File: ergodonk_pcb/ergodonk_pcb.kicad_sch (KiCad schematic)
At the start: 133 parts, among them J10 TRRS Double Sided, J11 Pimaroni Trackball, J12 Conn_01x04_Socket, Q1 TIP120, SW08_RH10 SW_PUSH_LED, SW1 SW_PUSH_LED, SW10 SW_PUSH_LED, SW11 SW_PUSH_LED, SW12 SW_PUSH_LED, SW13 SW_PUSH_LED, SW14 SW_PUSH_LED, SW15 SW_PUSH_LED, SW16 SW_PUSH_LED, SW17 SW_PUSH_LED, SW18_RH10 SW_PUSH_LED, SW2 SW_PUSH_LED, SW20 SW_PUSH_LED, SW21 SW_PUSH_LED, SW22 SW_PUSH_LED, SW23 SW_PUSH_LED, SW24 SW_PUSH_LED, SW25 SW_PUSH_LED, SW26 SW_PUSH_LED, SW27 SW_PUSH_LED, SW28_RH10 SW_PUSH_LED, SW3 SW_PUSH_LED, SW30 SW_PUSH_LED, SW31 SW_PUSH_LED, SW32 SW_PUSH_LED, SW33 SW_PUSH_LED, SW34 SW_PUSH_LED, SW35 SW_PUSH_LED, SW36 SW_PUSH_LED, SW37 SW_PUSH_LED, SW38_RH10 SW_PUSH_LED, SW4 SW_PUSH_LED, SW40 SW_PUSH_LED, SW42 SW_PUSH_LED, SW43 SW_PUSH_LED, SW44 SW_PUSH_LED, SW45 SW_PUSH_LED, SW46 SW_PUSH_LED, SW47 SW_PUSH_LED, SW48_RH10 SW_PUSH_LED, SW5 SW_PUSH_LED, SW50 SW_PUSH_LED, SW51 SW_PUSH_LED, SW52 SW_PUSH_LED, SW53 SW_PUSH_LED, SW54 SW_PUSH_LED, SW55 SW_PUSH_LED, SW56 SW_PUSH_LED, SW57 SW_PUSH_LED, SW58 SW_PUSH_LED, SW6 SW_PUSH_LED, SW7 SW_PUSH_LED, U10 Pico

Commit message: TRRS cleanup pimironi revision outline rework
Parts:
- removed J10: TRRS Double Sided, Resistor_SMD:R_1206_3216Metric_Pad1.30x1.75mm_HandSolder, symbol Ergodonk_symbols:TRRS_TX_to_RX_Doublesided_Crossover
- removed J11: Pimaroni Trackball, ergodonk_kicad_library:pimoroni_trackball, symbol Connector:Conn_01x05_Socket
- removed J12: Conn_01x04_Socket, symbol Connector:Conn_01x04_Socket
- added J1: TRRS, ergodonk_kicad_library:Cantor_DS_TRRS-PJ-320A, symbol keebio:TRRS
- added J10: Pimaroni Trackball, ergodonk_kicad_library:pimoroni_trackball, symbol Connector:Conn_01x05_Socket
- D_SOL_1: footprint Neffs_kicad_footprint_library:MUR340S_IN4004_TH -> kbd:R
- JP10: footprint (none) -> kbd:Jumper
- R12: footprint (none) -> kbd:R
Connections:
- net GND: now also J1.2 (TIP), J10.5 (Pin_5)
- net RX: now also J1.3 (RING1)
- net SCL: now also J10.3 (Pin_3)
- net SDA: now also J10.2 (Pin_2)
- net TX: now also J1.4 (RING2)
- net VCC: now also U10.36 (3V3); no longer U10.40 (VBUS)
- net at JP10.2 (B), R12.1: now also J10.1 (Pin_1)
- new net +3V3: J1.1 (SLEEVE)
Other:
- note added: "Todo: Check Pimaroni resistor calculation and footprint size Add holes to pimaroni footprint CHeck net trace sizes. (.5 for 3.3v?) Incree trcck size on vcc and GND nets Figure out VCC on Pico Figure out vbus_sense Cutouts for picon on PCB RH trackball Graphics Mouse bites Stabalizer holes Improve solenoid graphics Refactor key row/columns to put 00 in upper right for easier double sided Make Diod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"
- note removed: "Pimaroni Tie in (Additional Resistor?)"
- note removed: "Todo: pimaroni tie in additional pimroni resistor Incree trcck size on vcc and GND nets Figure out VCC on Pico Figure out vbus_sense Make new symbol for double sided TRRS Cutouts for picon on PCB Rewire for ProMicro footprint RH trackball Double sided RH/LH Add LEDs Graphics Mouse bites Stabalizer holes Improve solenoid graphics Refactor key row/columns to put 00 in upper right for easier double 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"

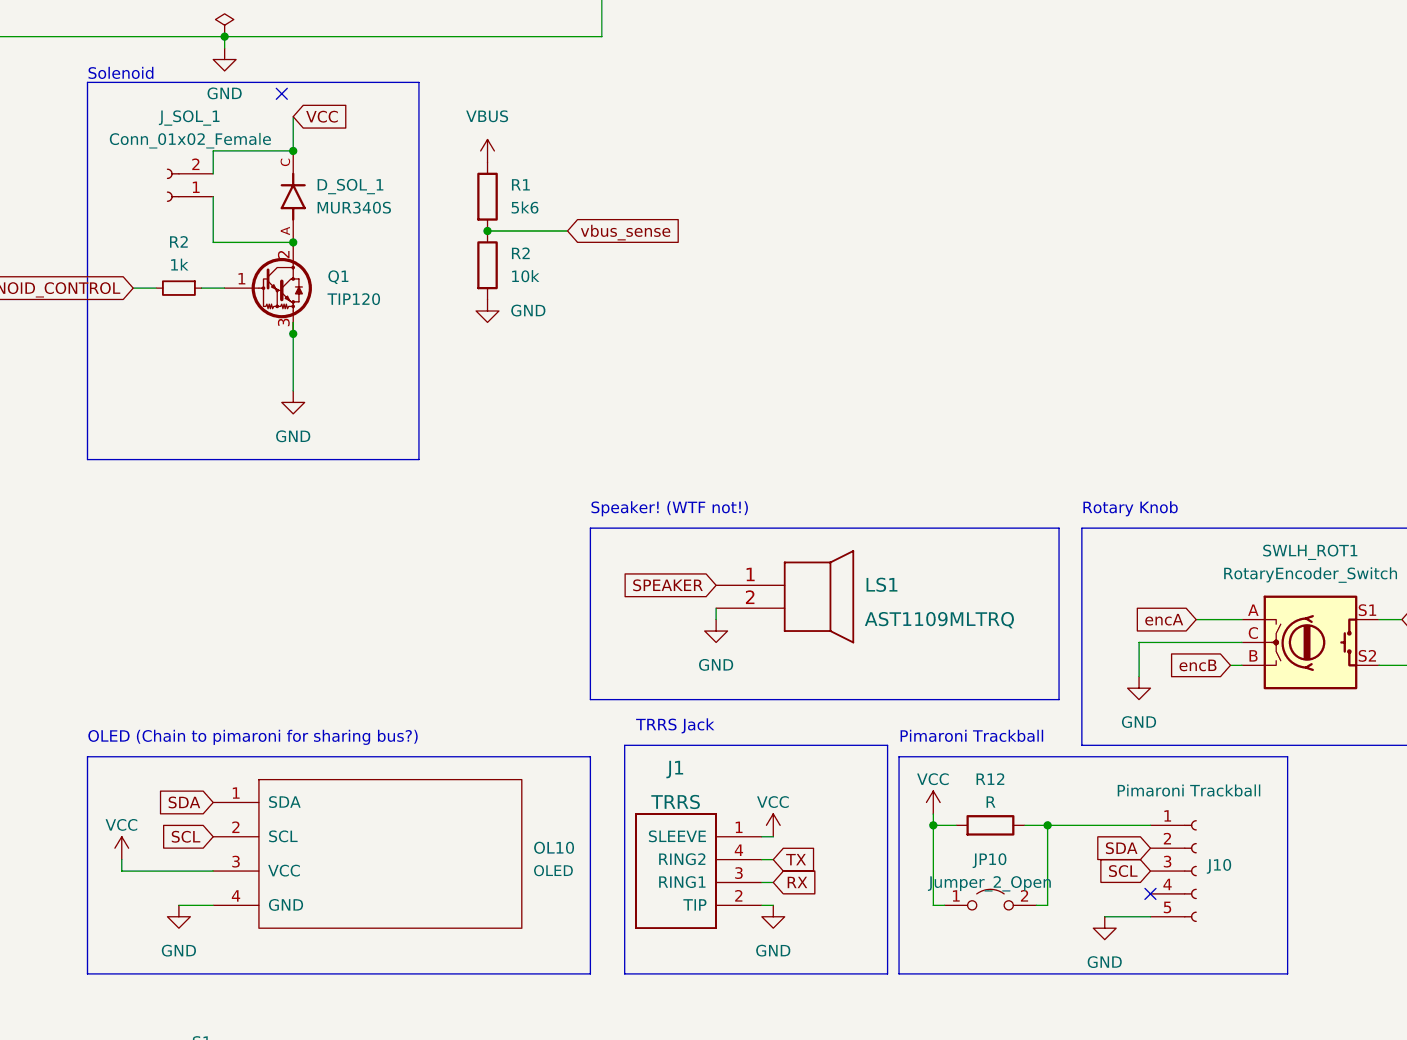
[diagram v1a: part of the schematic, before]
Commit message: Fixed MUR340 Hybrid footprint     Regenerated .dsn for autorouting
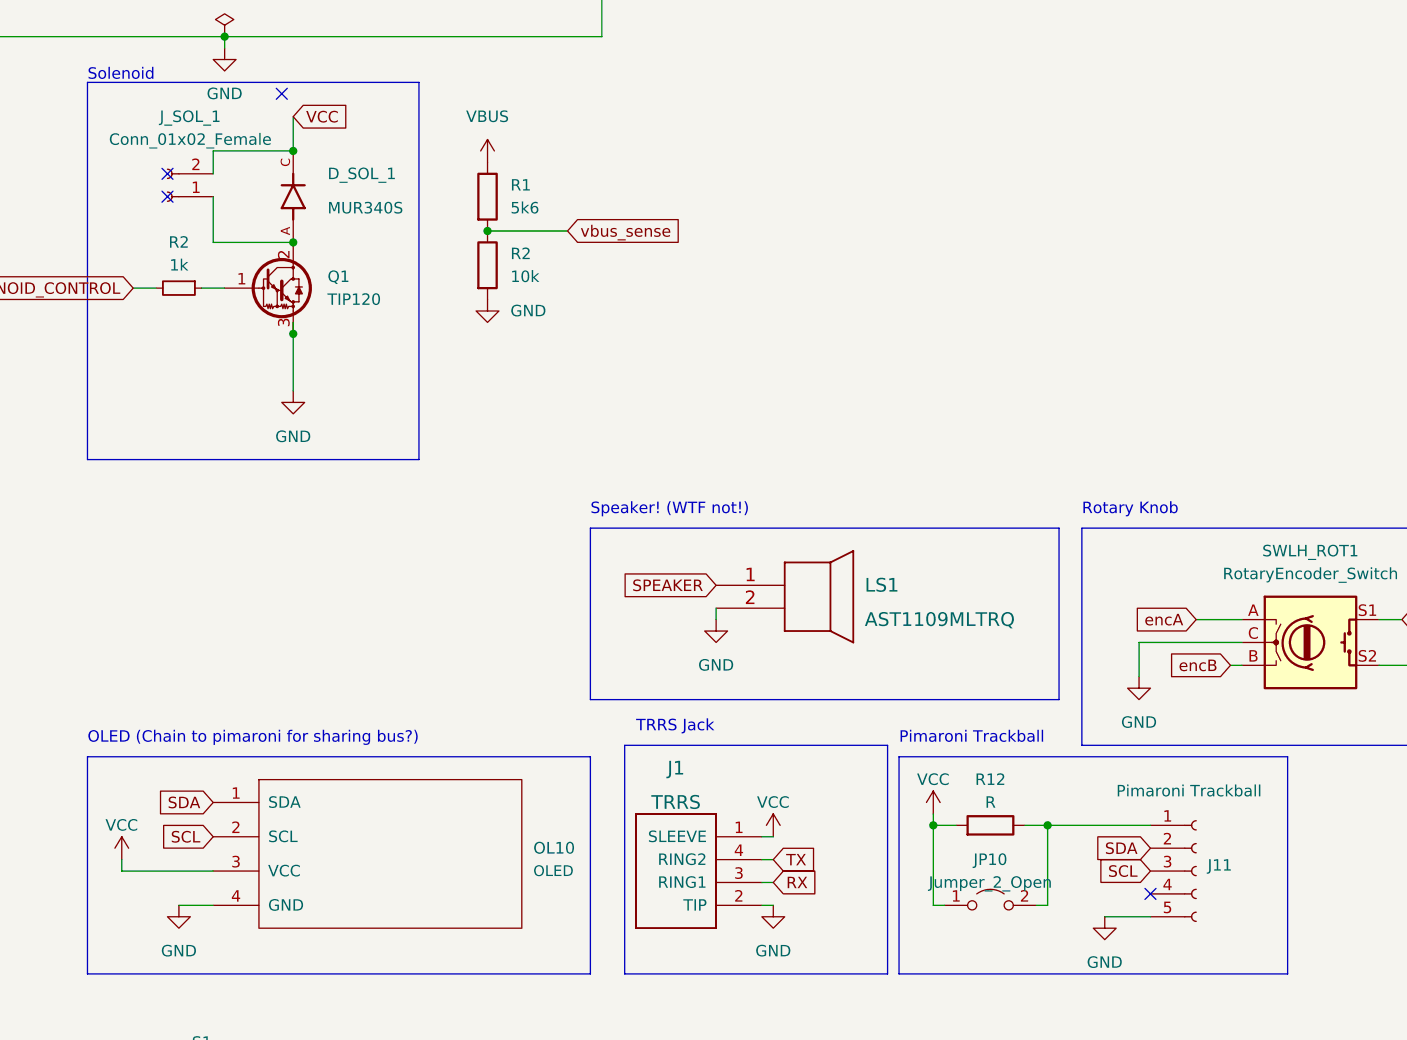
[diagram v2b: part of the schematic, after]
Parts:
- D_SOL_1: footprint kbd:R -> ergodonk_kicad_library:MUR340S_IN4004_TH
- renumbered J10 to J11
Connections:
- no-connect marks 2 -> 4
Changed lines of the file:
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@@
   )
   (no_connect (at 50.8 87.63))
+  (no_connect (at 38.1 99.06))
   (no_connect (at 147.32 176.53))
+  (no_connect (at 38.1 96.52))
   (wire (pts (xy 358.14 74.93) (xy 379.73 74.93))
     (stroke (width 0) (type default))
@@
   )
   (symbol (lib_id "MUR340S:MUR340S") (at 52.07 99.06 90) (unit 1)
-    (in_bom yes) (on_board yes) (dnp no) (fields_autoplaced)
-    (property "Reference" "D_SOL_1" (at 54.61 97.7899 90)
+    (in_bom yes) (on_board yes) (dnp no)
+    (property "Reference" "D_SOL_1" (at 55.88 96.52 90)
       (effects (font (size 1.27 1.27)) (justify right))
     )
-    (property "Value" "MUR340S" (at 54.61 100.3299 90)
+    (property "Value" "MUR340S" (at 55.88 100.33 90)
       (effects (font (size 1.27 1.27)) (justify right))
     )
-    (property "Footprint" "kbd:R" (at 52.07 99.06 0)
+    (property "Footprint" "ergodonk_kicad_library:MUR340S_IN4004_TH" (at 52.07 99.06 0)
       (effects (font (size 1.27 1.27)) (justify bottom) hide)
     )
@@
   (symbol (lib_id "Connector:Conn_01x05_Socket") (at 152.4 173.99 0) (unit 1)
     (in_bom yes) (on_board yes) (dnp no)
-    (property "Reference" "J10" (at 153.67 173.355 0)
+    (property "Reference" "J11" (at 153.67 173.355 0)
       (effects (font (size 1.27 1.27)) (justify left))
     )
@@
       (project "ergodonk_pcb"
         (path "/ed1aaf15-4e1f-4159-b371-d99b3fb972ad"
-          (reference "J10") (unit 1)
+          (reference "J11") (unit 1)
         )
       )

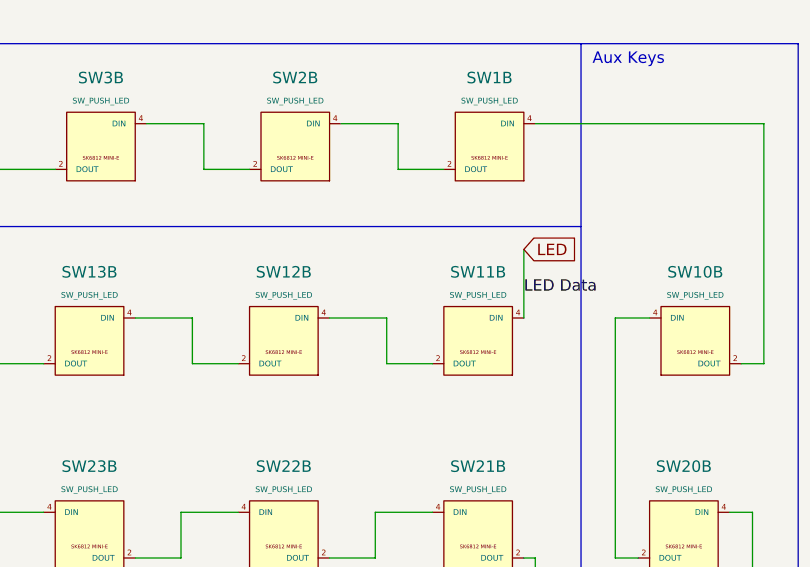
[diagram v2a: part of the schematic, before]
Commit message: Added zones Wired VCC to VDD for LED Regenerated dsn for autorouting
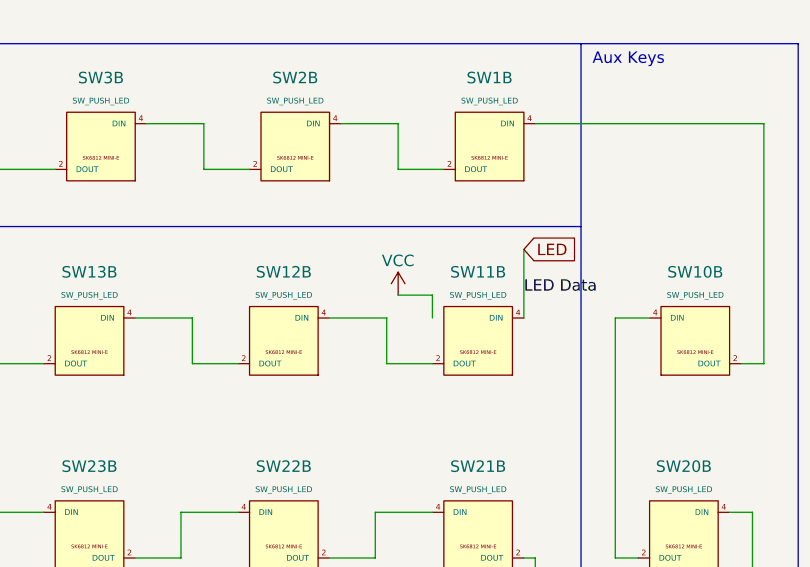
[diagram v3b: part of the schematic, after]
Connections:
- net VDD is gone; now on net VCC: SW08_RH10.1 (VDD), SW1.1 (VDD), SW10.1 (VDD), SW11.1 (VDD), SW12.1 (VDD), SW13.1 (VDD), SW14.1 (VDD), SW15.1 (VDD), SW16.1 (VDD), SW17.1 (VDD), SW18_RH10.1 (VDD), SW2.1 (VDD), SW20.1 (VDD), SW21.1 (VDD), SW22.1 (VDD), SW23.1 (VDD), SW24.1 (VDD), SW25.1 (VDD), SW26.1 (VDD), SW27.1 (VDD), SW28_RH10.1 (VDD), SW3.1 (VDD), SW30.1 (VDD), SW31.1 (VDD), SW32.1 (VDD), SW33.1 (VDD), SW34.1 (VDD), SW35.1 (VDD), SW36.1 (VDD), SW37.1 (VDD), SW38_RH10.1 (VDD), SW4.1 (VDD), SW40.1 (VDD), SW42.1 (VDD), SW43.1 (VDD), SW44.1 (VDD), SW45.1 (VDD), SW46.1 (VDD), SW47.1 (VDD), SW48_RH10.1 (VDD), SW5.1 (VDD), SW50.1 (VDD), SW51.1 (VDD), SW52.1 (VDD), SW53.1 (VDD), SW54.1 (VDD), SW55.1 (VDD), SW56.1 (VDD), SW57.1 (VDD), SW58.1 (VDD), SW6.1 (VDD), SW7.1 (VDD)
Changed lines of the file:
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@@
     (stroke (width 0) (type default))
   )
+  (wire (pts (xy 358.14 -133.35) (xy 361.95 -133.35))
+    (stroke (width 0) (type default))
+  )
   (wire (pts (xy 314.96 138.43) (xy 314.96 139.7))
     (stroke (width 0) (type default))
@@
     (stroke (width 0) (type default))
   )
+  (wire (pts (xy 361.95 -133.35) (xy 361.95 -130.81))
+    (stroke (width 0) (type default))
+  )
   (wire (pts (xy 213.36 67.31) (xy 213.36 45.72))
     (stroke (width 0) (type default))
@@
         )
       )
+    )
+  )
+  (symbol (lib_name "VCC_2") (lib_id "power:VCC") (at 358.14 -133.35 0) (unit 1)
+    (in_bom yes) (on_board yes) (dnp no)
+    (property "Reference" "#PWR012" (at 358.14 -129.54 0)
+      (effects (font (size 1.27 1.27)) hide)
+    )
+    (property "Value" "VCC" (at 358.14 -137.16 0)
+      (effects (font (size 1.27 1.27)))
+    )
+    (property "Footprint" "" (at 358.14 -133.35 0)
+      (effects (font (size 1.27 1.27)) hide)
+    )
+    (property "Datasheet" "" (at 358.14 -133.35 0)
+      (effects (font (size 1.27 1.27)) hide)
+    )
+    (pin "1")
+    (instances
+      (project "ergodonk_pcb"
+        (path "/ed1aaf15-4e1f-4159-b371-d99b3fb972ad"
+          (reference "#PWR012") (unit 1)
+        )
+      )
